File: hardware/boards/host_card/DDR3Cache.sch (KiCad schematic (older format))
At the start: 6 parts, among them U1 ECP5UM5G-381caBGA, U4 IS43TR16256B-125KBL, X2 AX3

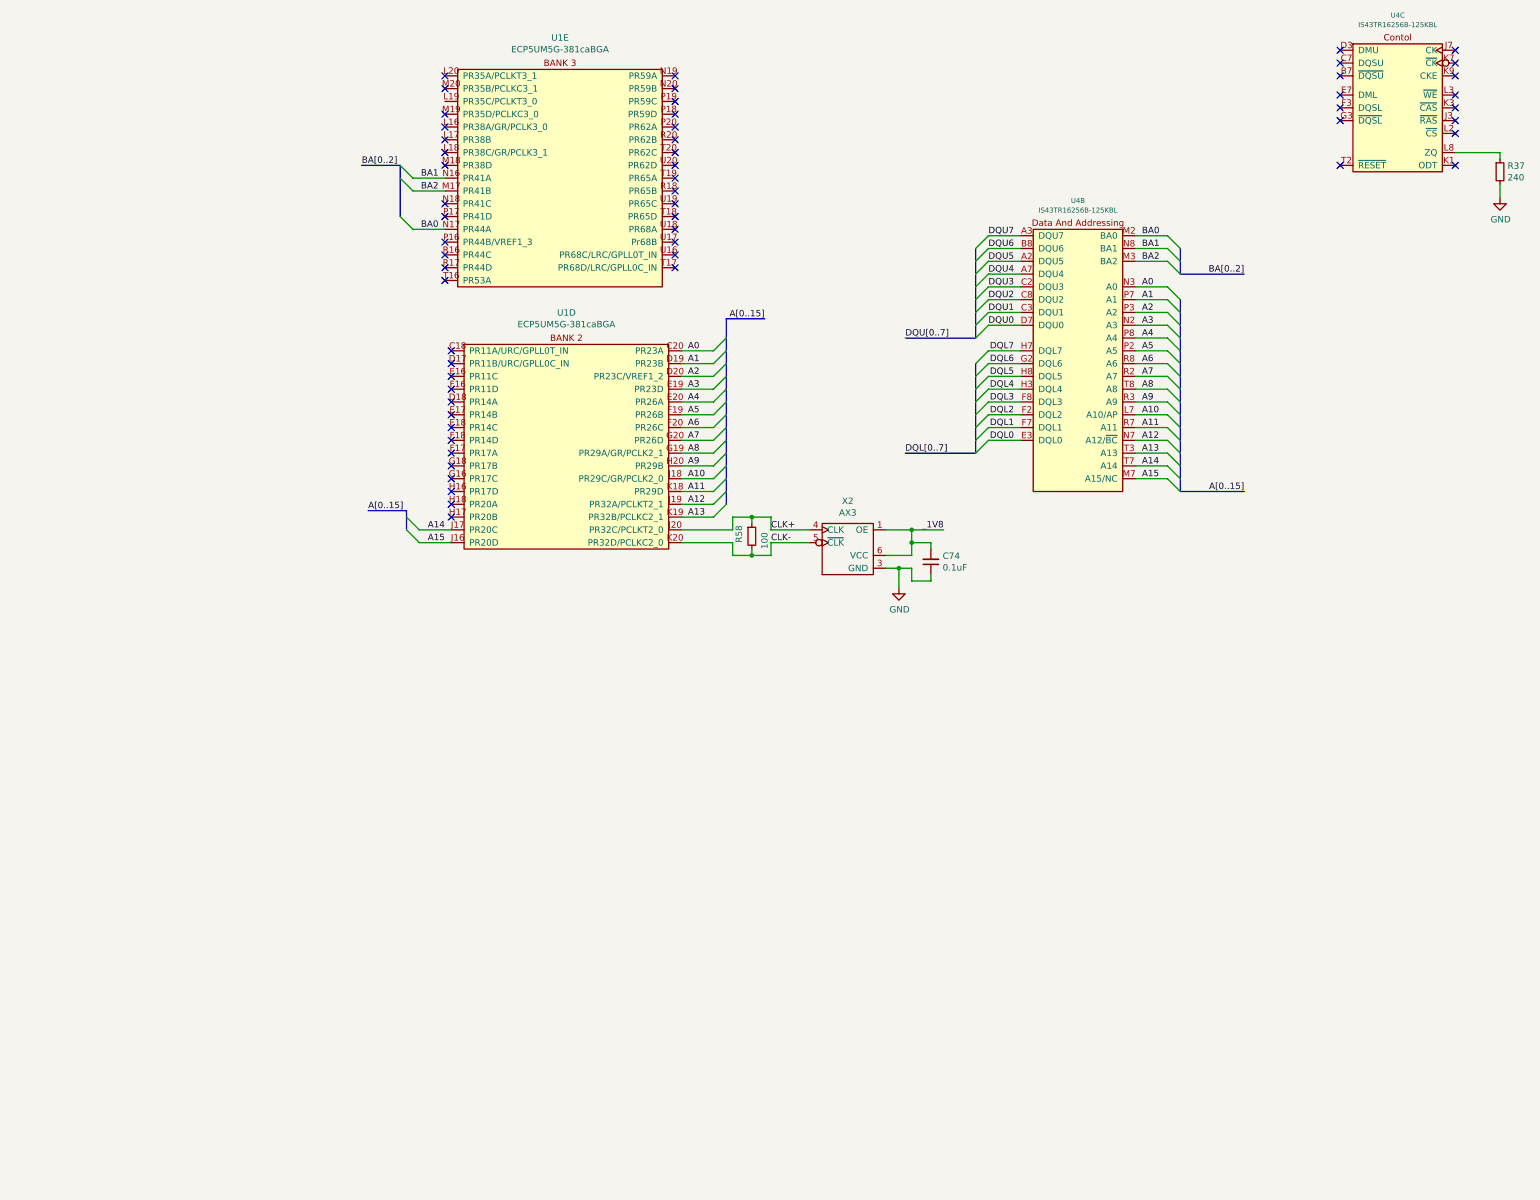
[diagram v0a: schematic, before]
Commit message: Added another DDR3 module to expand cache to 8GiB
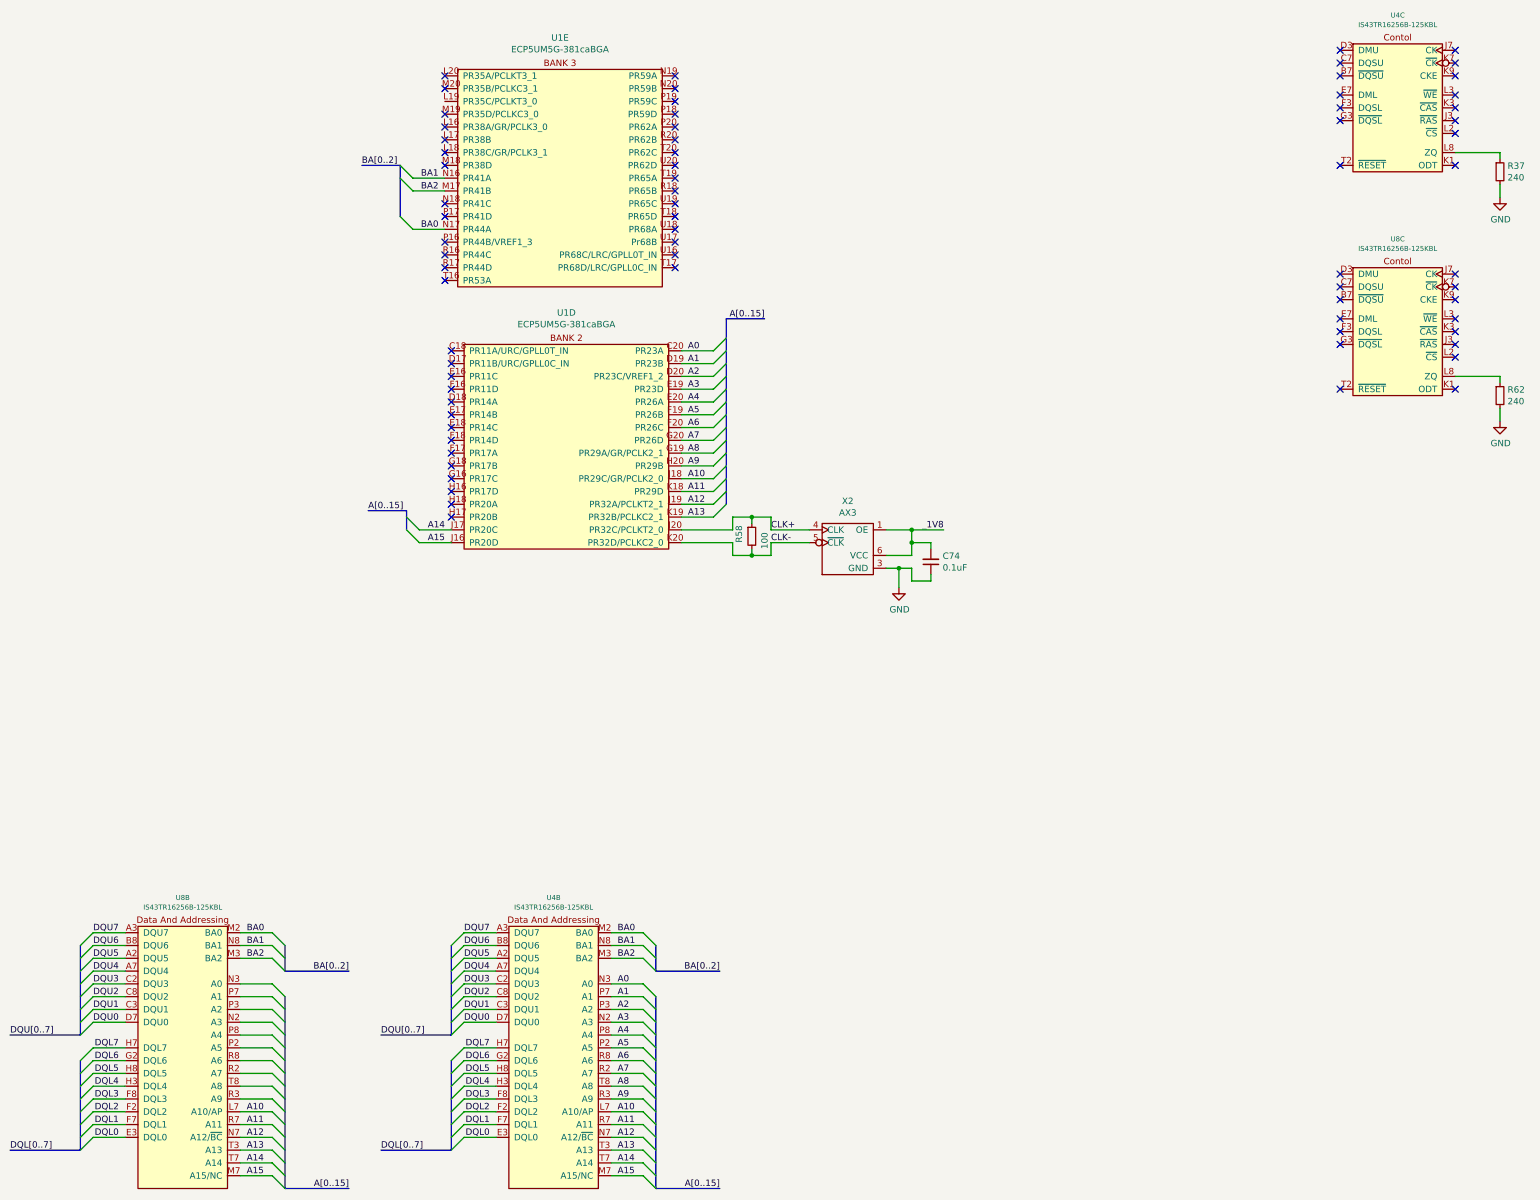
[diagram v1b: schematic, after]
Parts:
- added R62: 240, Resistor_SMD:R_0603_1608Metric, symbol Device:R_Small
- added U8: IS43TR16256B-125KBL, Package_BGA:BGA-96_9.0x13.0mm_Layout2x3x16_P0.8mm, symbol lethalbit-memory:IS43TR16256B-125KBL
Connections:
- net A10: now also U8.L7 (A10/AP)
- net A11: now also U8.R7 (A11)
- net A12: now also U8.N7 (A12/~BC)
- net A13: now also U8.T3 (A13)
- net A14: now also U8.T7 (A14)
- net A15: now also U8.M7 (A15/NC)
- net BA0: now also U8.M2 (BA0)
- net BA1: now also U8.N8 (BA1)
- net BA2: now also U8.M3 (BA2)
- net DQL0: now also U8.E3 (DQL0)
- net DQL1: now also U8.F7 (DQL1)
- net DQL2: now also U8.F2 (DQL2)
- net DQL3: now also U8.F8 (DQL3)
- net DQL4: now also U8.H3 (DQL4)
- net DQL5: now also U8.H8 (DQL5)
- net DQL6: now also U8.G2 (DQL6)
- net DQL7: now also U8.H7 (DQL7)
- net DQU0: now also U8.D7 (DQU0)
- net DQU1: now also U8.C3 (DQU1)
- net DQU2: now also U8.C8 (DQU2)
- net DQU3: now also U8.C2 (DQU3)
- net DQU4: now also U8.A7 (DQU4)
- net DQU5: now also U8.A2 (DQU5)
- net DQU6: now also U8.B8 (DQU6)
- net DQU7: now also U8.A3 (DQU7)
- net GND: now also R62.2
- new net: R62.1, U8.L8 (ZQ)
- no-connect marks 58 -> 73
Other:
- moved on the sheet: U4B
